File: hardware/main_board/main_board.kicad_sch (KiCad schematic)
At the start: 96 parts, among them J1 USB_C_Receptacle_USB2.0_16P, J3 BAT1, J4 Conn_02x05_Odd_Even, J5 Conn_02x05_Odd_Even, Q1 MMBT3904, Q17 FDMC4435BZ, Q2 MMBT3904, SW1 PTS645VK31LFS, SW2 PTS645VK31LFS, SW3 PTS645VK31LFS, U10 HUSB238_002DD, U11 TPS22810DBVR, U12 TPS2121, U14 BQ25601, U15 TPS63802, U17 NCH2800HV, U2 CP2102N-A02-GQFN28, U3 SRV05-4, U4 DFPlayer_mini, U5 ESP32-S3-WROOM1, U6 DS3231MZ, U7 TPS22918DBVR, U9 TPS61022

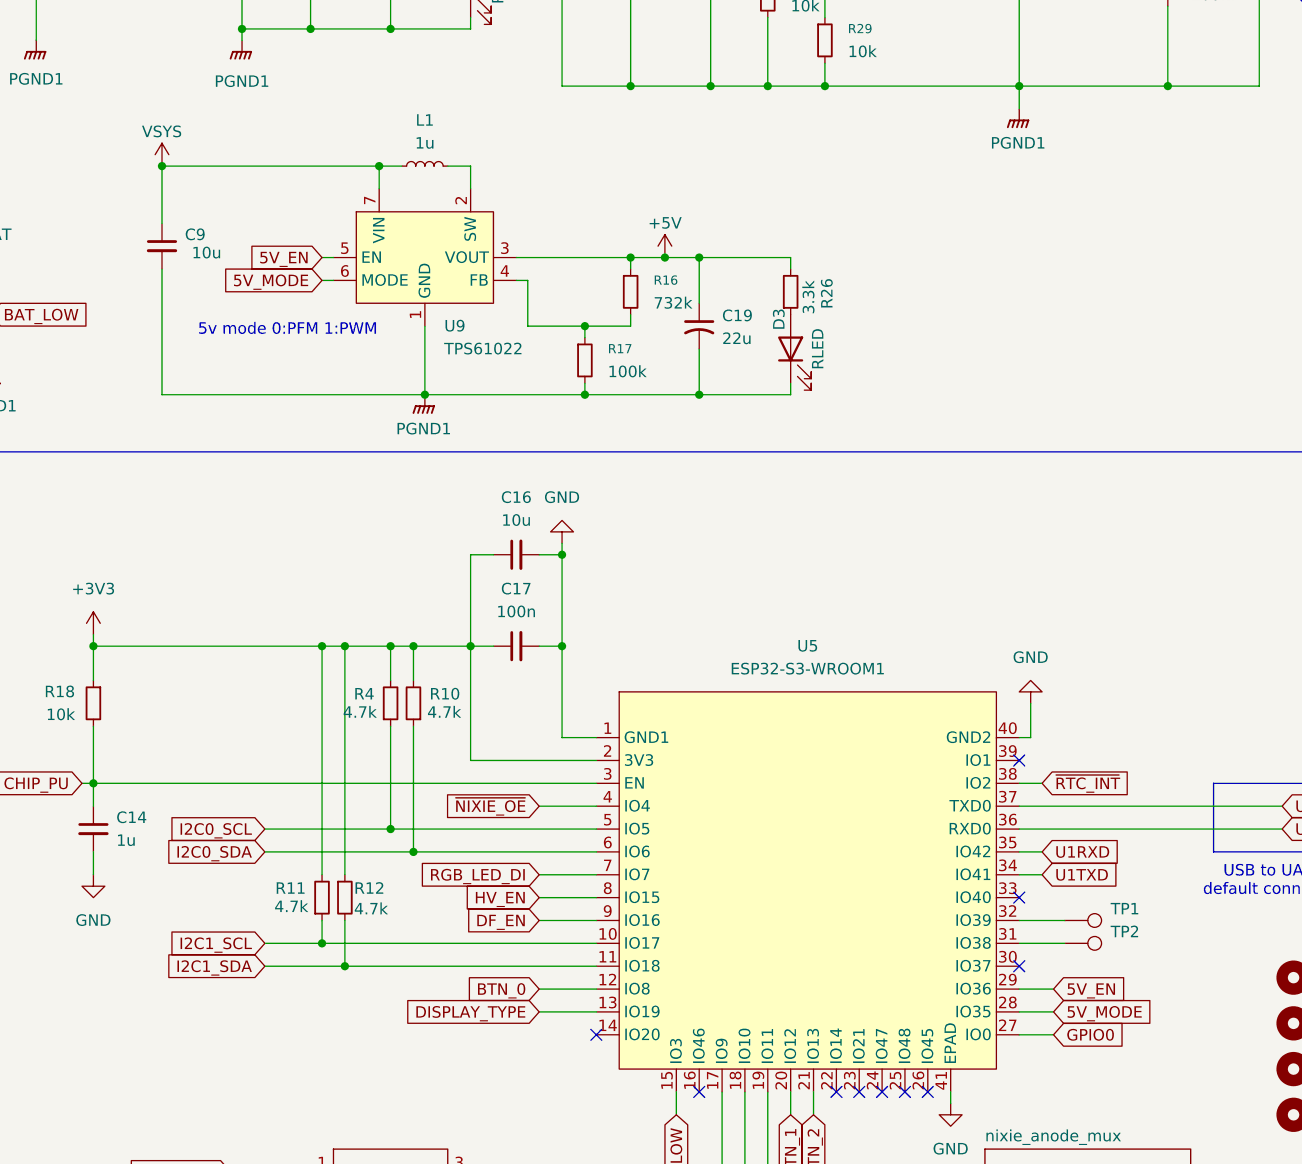
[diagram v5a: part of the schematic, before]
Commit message: chore(hw): update 5V boost circuit, always enable
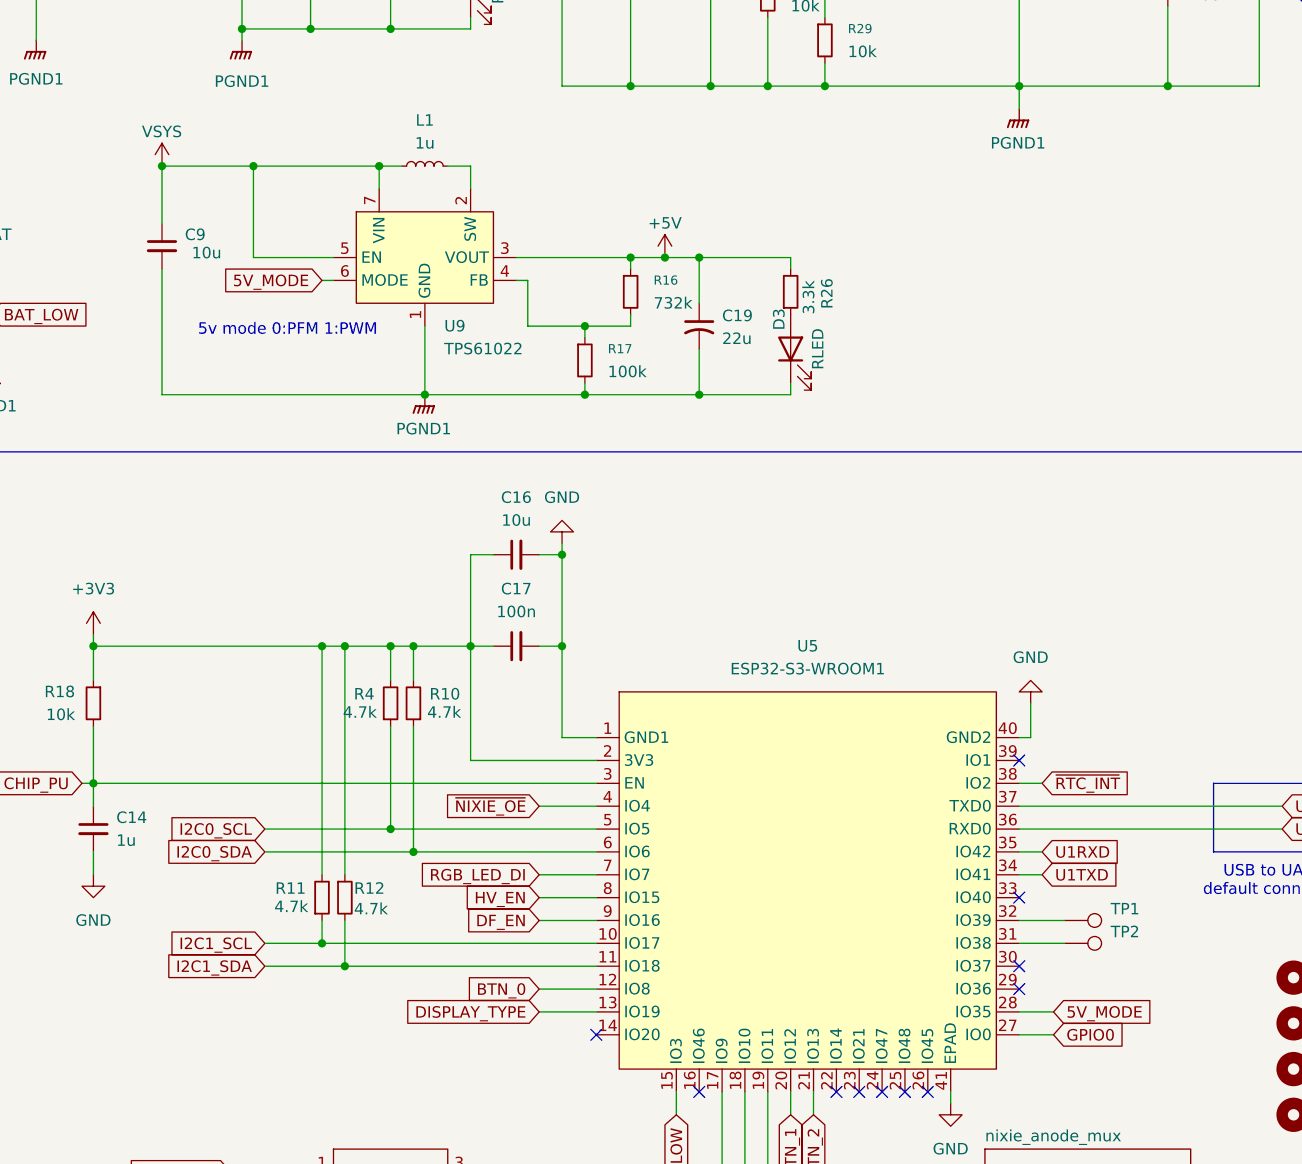
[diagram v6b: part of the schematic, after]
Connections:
- net VSYS: now also U9.5 (EN)
- net 5V_EN: no longer names the net of U5.29 (IO36)
- net 5V_EN: no longer U9.5 (EN)
- no-connect marks 46 -> 47
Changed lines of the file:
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@@
 	)
 	(junction
+		(at 259.08 69.85)
+		(diameter 0)
+		(color 0 0 0 0)
+	)
+	(junction
 		(at 295.91 87.63)
 		(diameter 0)
@@
 	)
 	(no_connect
+		(at 344.17 161.29)
+	)
+	(no_connect
 		(at 182.88 237.49)
 	)
@@
 	(wire
 		(pts
-			(xy 248.92 69.85) (xy 273.05 69.85)
+			(xy 248.92 69.85) (xy 259.08 69.85)
 		)
 		(stroke
@@
 	(wire
 		(pts
+			(xy 259.08 69.85) (xy 273.05 69.85)
+		)
+		(stroke
+			(width 0)
+			(type default)
+		)
+	)
+	(wire
+		(pts
 			(xy 300.99 20.32) (xy 300.99 21.59)
 		)
@@
 	(wire
 		(pts
-			(xy 167.64 41.91) (xy 167.64 46.99)
+			(xy 259.08 80.01) (xy 267.97 80.01)
 		)
 		(stroke
@@
 	(wire
 		(pts
-			(xy 146.05 115.57) (xy 148.59 115.57)
+			(xy 167.64 41.91) (xy 167.64 46.99)
 		)
 		(stroke
@@
 	(wire
 		(pts
-			(xy 149.86 240.03) (xy 149.86 237.49)
+			(xy 146.05 115.57) (xy 148.59 115.57)
 		)
 		(stroke
@@
 	(wire
 		(pts
-			(xy 293.37 123.19) (xy 293.37 133.35)
+			(xy 149.86 240.03) (xy 149.86 237.49)
 		)
 		(stroke
@@
 	(wire
 		(pts
-			(xy 356.87 38.1) (xy 360.68 38.1)
+			(xy 293.37 123.19) (xy 293.37 133.35)
 		)
 		(stroke
@@
 	(wire
 		(pts
-			(xy 363.22 200.66) (xy 382.27 200.66)
+			(xy 356.87 38.1) (xy 360.68 38.1)
 		)
 		(stroke
@@
 	(wire
 		(pts
-			(xy 226.06 86.36) (xy 229.87 86.36)
+			(xy 363.22 200.66) (xy 382.27 200.66)
 		)
 		(stroke
@@
 	(wire
 		(pts
-			(xy 257.81 54.61) (xy 257.81 55.88)
+			(xy 226.06 86.36) (xy 229.87 86.36)
 		)
 		(stroke
@@
 	(wire
 		(pts
-			(xy 266.7 80.01) (xy 267.97 80.01)
+			(xy 257.81 54.61) (xy 257.81 55.88)
 		)
 		(stroke
@@
 	(wire
 		(pts
+			(xy 259.08 80.01) (xy 259.08 69.85)
+		)
+		(stroke
+			(width 0)
+			(type default)
+		)
+	)
+	(wire
+		(pts
 			(xy 274.32 45.72) (xy 274.32 54.61)
 		)
@@
 	(wire
 		(pts
-			(xy 344.17 161.29) (xy 347.98 161.29)
-		)
-		(stroke
-			(width 0)
-			(type default)
-		)
-	)
-	(wire
-		(pts
 			(xy 102.87 26.67) (xy 106.68 26.67)
 		)
@@
 		)
 	)
-	(global_label "5V_EN"
-		(shape input)
-		(at 266.7 80.01 180)
-		(fields_autoplaced yes)
-		(effects
-			(font
-				(size 1.27 1.27)
-			)
-			(justify right)
-		)
-		(property "Intersheetrefs" "${INTERSHEET_REFS}"
-			(at 257.9696 80.01 0)
-			(effects
-				(font
-					(size 1.27 1.27)
-				)
-				(justify right)
-				(hide yes)
-			)
-		)
-	)
 	(global_label "I2C0_SCL"
 		(shape input)
@@
 			(effects
 				(font
-					(size 1.27 1.27)
-				)
-				(justify left)
-				(hide yes)
-			)
-		)
-	)
-	(global_label "5V_EN"
-		(shape input)
-		(at 347.98 161.29 0)
-		(fields_autoplaced yes)
-		(effects
-			(font
-				(size 1.27 1.27)
-			)
-			(justify left)
-		)
-		(property "Intersheetrefs" "${INTERSHEET_REFS}"
-			(at 356.7104 161.29 0)
-			(effects
-				(font

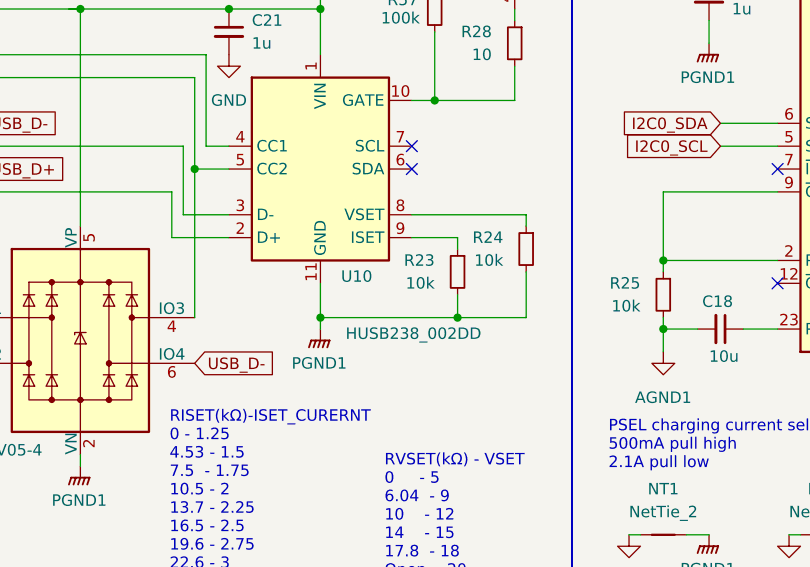
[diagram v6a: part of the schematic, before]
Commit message: chore(hw): update HUSB238 current setting resistor from 10k to 10.5k
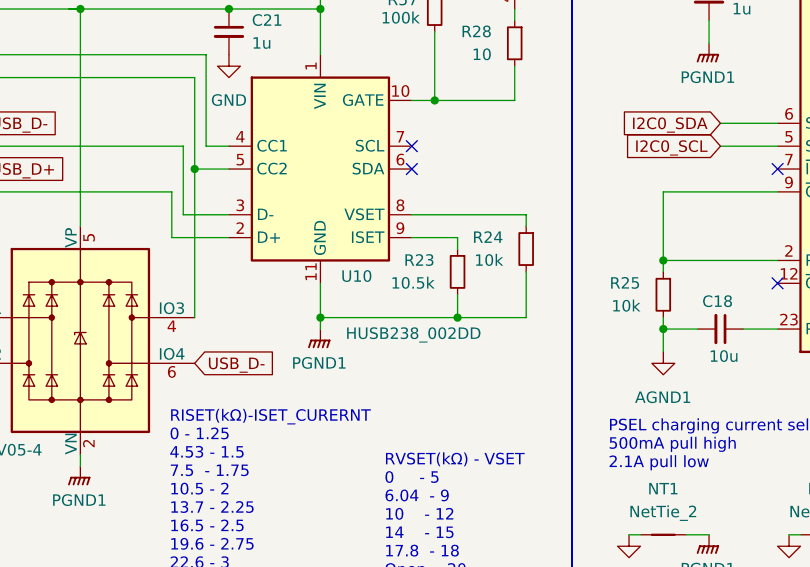
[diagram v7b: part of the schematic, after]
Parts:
- R23: value 10k -> 10.5k; LCSC PN C25744 -> C22855
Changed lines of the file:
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@@
 			)
 		)
-		(property "Value" "10k"
+		(property "Value" "10.5k"
 			(at 102.87 64.7699 0)
 			(effects
@@
 			)
 		)
-		(property "LCSC PN" "C25744"
+		(property "LCSC PN" "C22855"
 			(at 105.41 63.5 90)
 			(effects

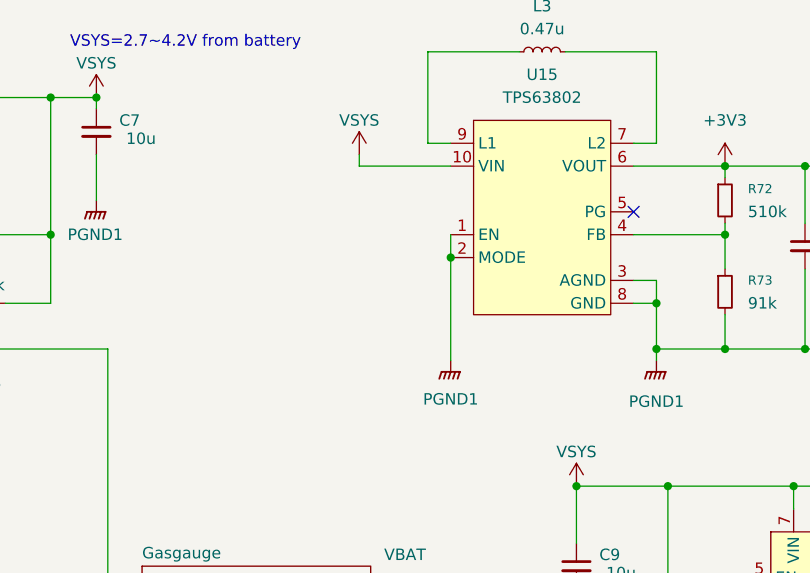
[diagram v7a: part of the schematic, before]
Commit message: fix(hw): fix TPS63802 EN pin and MODE pin to always high (always enable and PWM mode), add titanium bulk capacitor for TPS61022 to prevent the input oscillation by datasheet noticed
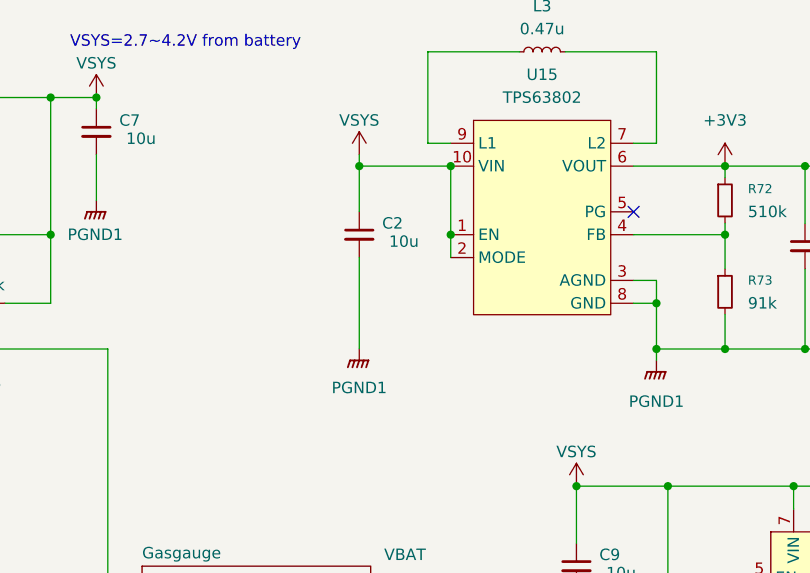
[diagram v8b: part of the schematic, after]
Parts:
- added C2: 10u, Capacitor_Tantalum_SMD:CP_EIA-2012-12_Kemet-R, symbol Device:C_Small
- C9: footprint Capacitor_SMD:C_0805_2012Metric -> Capacitor_Tantalum_SMD:CP_EIA-2012-12_Kemet-R; LCSC PN C6119932 -> C129234
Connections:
- net PGND1: now also C2.2; no longer U15.1 (EN), U15.2 (MODE)
- net VSYS: now also U15.1 (EN), U15.2 (MODE), C2.1
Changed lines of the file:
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@@
 	)
 	(junction
+		(at 234.95 41.91)
+		(diameter 0)
+		(color 0 0 0 0)
+	)
+	(junction
 		(at 355.6 29.21)
 		(diameter 0)
@@
 	)
 	(junction
-		(at 234.95 44.45)
-		(diameter 0)
-		(color 0 0 0 0)
-	)
-	(junction
 		(at 63.5 34.29)
 		(diameter 0)
@@
 	)
 	(junction
+		(at 234.95 34.29)
+		(diameter 0)
+		(color 0 0 0 0)
+	)
+	(junction
 		(at 133.35 26.67)
 		(diameter 0)
@@
 	)
 	(junction
+		(at 224.79 34.29)
+		(diameter 0)
+		(color 0 0 0 0)
+	)
+	(junction
 		(at 76.2 52.07)
 		(diameter 0)
@@
 	(wire
 		(pts
-			(xy 234.95 44.45) (xy 234.95 55.88)
-		)
-		(stroke
-			(width 0)
-			(type default)
-		)
-	)
-	(wire
-		(pts
 			(xy 295.91 88.9) (xy 295.91 87.63)
 		)
@@
 	(wire
 		(pts
-			(xy 234.95 41.91) (xy 234.95 44.45)
-		)
-		(stroke
-			(width 0)
-			(type default)
-		)
-	)
-	(wire
-		(pts
 			(xy 316.23 39.37) (xy 316.23 38.1)
 		)
@@
 	(wire
 		(pts
+			(xy 234.95 41.91) (xy 234.95 44.45)
+		)
+		(stroke
+			(width 0)
+			(type default)
+		)
+	)
+	(wire
+		(pts
 			(xy 25.4 73.66) (xy 29.21 73.66)
 		)
@@
 	(wire
 		(pts
+			(xy 224.79 34.29) (xy 224.79 39.37)
+		)
+		(stroke
+			(width 0)
+			(type default)
+		)
+	)
+	(wire
+		(pts
 			(xy 360.68 52.07) (xy 360.68 60.96)
 		)
@@
 	(wire
 		(pts
+			(xy 224.79 44.45) (xy 224.79 54.61)
+		)
+		(stroke
+			(width 0)
+			(type default)
+		)
+	)
+	(wire
+		(pts
 			(xy 363.22 193.04) (xy 369.57 193.04)
 		)
@@
 	(wire
 		(pts
+			(xy 234.95 34.29) (xy 234.95 41.91)
+		)
+		(stroke
+			(width 0)
+			(type default)
+		)
+	)
+	(wire
+		(pts
 			(xy 138.43 227.33) (xy 137.16 227.33)
 		)
@@
 	(symbol
 		(lib_id "power:GNDPWR")
-		(at 234.95 55.88 0)
+		(at 224.79 54.61 0)
 		(unit 1)
 		(exclude_from_sim no)
@@
 		(dnp no)
 		(property "Reference" "#PWR086"
-			(at 234.95 60.96 0)
+			(at 224.79 59.69 0)
 			(effects
 				(font
@@
 		)
 		(property "Value" "PGND1"
-			(at 234.95 60.198 0)
+			(at 224.79 58.928 0)
 			(effects
 				(font
@@
 		)
 		(property "Footprint" ""
-			(at 234.95 57.15 0)
+			(at 224.79 55.88 0)
 			(effects
 				(font
@@
 		)
 		(property "Datasheet" ""
-			(at 234.95 57.15 0)
+			(at 224.79 55.88 0)
 			(effects
 				(font
@@
 		)
 		(property "Description" "Power symbol creates a global label with name \"GNDPWR\" , global ground"
-			(at 234.95 55.88 0)
+			(at 224.79 54.61 0)
 			(effects
 				(font
@@
 	)
 	(symbol
+		(lib_id "Device:C_Small")
+		(at 224.79 41.91 0)
+		(unit 1)
+		(exclude_from_sim no)
+		(in_bom yes)
+		(on_board yes)
+		(dnp no)
+		(property "Reference" "C2"
+			(at 227.33 40.6463 0)
+			(effects
+				(font
+					(size 1.27 1.27)
+				)
+				(justify left)
+			)
+		)
+		(property "Value" "10u"
+			(at 228.092 42.672 0)
+			(effects
+				(font
+					(size 1.27 1.27)
+				)
+				(justify left)
+			)
+		)
+		(property "Footprint" "Capacitor_Tantalum_SMD:CP_EIA-2012-12_Kemet-R"
+			(at 224.79 41.91 0)
+			(effects
+				(font
+					(size 1.27 1.27)
+				)
+				(hide yes)
+			)
+		)
+		(property "Datasheet" "~"
+			(at 224.79 41.91 0)
+			(effects
+				(font
+					(size 1.27 1.27)
+				)
+				(hide yes)
+			)
+		)
+		(property "Description" "10uF/10V"
+			(at 224.79 41.91 0)
+			(effects
+				(font
+					(size 1.27 1.27)
+				)
+				(hide yes)
+			)
+		)
+		(property "LCSC PN" "C129234"
+			(at 224.79 41.91 0)
+			(effects
+				(font
+					(size 1.27 1.27)
+				)
+				(hide yes)
+			)
+		)
+		(pin "1"
+		)
+		(pin "2"
+		)
+		(instances
+			(project "main_board"
+				(path "/62950e93-3f98-4dee-9256-8213caa98ee7"
+					(reference "C2")
+					(unit 1)
+				)
+			)
+		)
+	)
+	(symbol
 		(lib_id "power:GND")
 		(at 60.96 26.67 0)
@@
 			)
 		)
-		(property "Footprint" "Capacitor_SMD:C_0805_2012Metric"
+		(property "Footprint" "Capacitor_Tantalum_SMD:CP_EIA-2012-12_Kemet-R"
 			(at 248.92 78.74 0)
 			(effects
@@
 			)
 		)
-		(property "Description" "10uF/25V"
+		(property "Description" "10uF/10V"
 			(at 248.92 78.74 0)
 			(effects
@@
 			)
 		)
-		(property "LCSC PN" "C6119932"
+		(property "LCSC PN" "C129234"
 			(at 248.92 78.74 0)
 			(effects
